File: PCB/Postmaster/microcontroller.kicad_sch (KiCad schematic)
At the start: 3 parts, among them U2 STM32F407VETx, Y1 TFOM50M4RWKCKT2T

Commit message: Update schematics
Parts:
- added U3: S25FL064LABMFI013, Package_SO:SOIC-8_5.23x5.23mm_P1.27mm, symbol Memory_Flash:W25Q16JVSS
- added Y2: CSTNE8M00G550000R0, Crystal:Resonator_SMD_Murata_CSTxExxV-3Pin_3.0x1.1mm, symbol Device:Resonator
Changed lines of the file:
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@@
 		(shape output)
 		(at 161.29 115.57 0)
+		(fields_autoplaced yes)
 		(effects
 			(font
@@
 		(shape output)
 		(at 184.15 41.91 0)
+		(fields_autoplaced yes)
 		(effects
 			(font
@@
 		(shape output)
 		(at 161.29 57.15 0)
+		(fields_autoplaced yes)
 		(effects
 			(font
@@
 		(shape output)
 		(at 161.29 110.49 0)
+		(fields_autoplaced yes)
 		(effects
 			(font
@@
 		(shape bidirectional)
 		(at 161.29 44.45 0)
+		(fields_autoplaced yes)
 		(effects
 			(font
@@
 		(shape output)
 		(at 161.29 113.03 0)
+		(fields_autoplaced yes)
 		(effects
 			(font
@@
 		(shape input)
 		(at 161.29 138.43 0)
+		(fields_autoplaced yes)
 		(effects
 			(font
@@
 		(shape input)
 		(at 161.29 135.89 0)
+		(fields_autoplaced yes)
 		(effects
 			(font
@@
 		(shape output)
 		(at 161.29 128.27 0)
-		(effects
-			(font
-				(size 1.27 1.27)
-			)
-			(justify left)
+		(fields_autoplaced yes)
+		(effects
+			(font
+				(size 1.27 1.27)
+			)
+			(justify left)
+		)
+	)
+	(symbol
+		(lib_id "Device:Resonator")
+		(at 205.74 92.71 0)
+		(unit 1)
+		(exclude_from_sim no)
+		(in_bom yes)
+		(on_board yes)
+		(dnp no)
+		(fields_autoplaced yes)
+		(property "Reference" "Y2"
+			(at 205.74 85.09 0)
+			(effects
+				(font
+					(size 1.27 1.27)
+				)
+			)
+		)
+		(property "Value" "CSTNE8M00G550000R0"
+			(at 205.74 87.63 0)
+			(effects
+				(font
+					(size 1.27 1.27)
+				)
+			)
+		)
+		(property "Footprint" "Crystal:Resonator_SMD_Murata_CSTxExxV-3Pin_3.0x1.1mm"
+			(at 205.105 92.71 0)
+			(effects
+				(font
+					(size 1.27 1.27)
+				)
+				(hide yes)
+			)
+		)
+		(property "Datasheet" "~"
+			(at 205.105 92.71 0)
+			(effects
+				(font
+					(size 1.27 1.27)
+				)
+				(hide yes)
+			)
+		)
+		(property "Description" "Three pin ceramic resonator"
+			(at 205.74 92.71 0)
+			(effects
+				(font
+					(size 1.27 1.27)
+				)
+				(hide yes)
+			)
+		)
+		(property "JLCPCBPart" "C341522"
+			(at 205.74 92.71 0)
+			(effects
+				(font
+					(size 1.27 1.27)
+				)
+				(hide yes)
+			)
+		)
+		(pin "2"
+		)
+		(pin "3"
+		)
+		(pin "1"
+		)
+		(instances
+			(project ""
+				(path "/b2fb7ca8-b44b-45c2-b25e-cd50f2bbc5c4/6b6c9333-359e-485e-9820-666d3b2f9ba5"
+					(reference "Y2")
+					(unit 1)
+				)
+			)
 		)
 	)
@@
 					(unit 1)
 				)
+			)
+		)
+	)
+	(symbol
+		(lib_id "Memory_Flash:W25Q16JVSS")
+		(at 208.28 127 0)
+		(unit 1)
+		(exclude_from_sim no)
+		(in_bom yes)
+		(on_board yes)
+		(dnp no)
+		(fields_autoplaced yes)
+		(property "Reference" "U3"
+			(at 217.17 125.7299 0)
+			(effects
+				(font
+					(size 1.27 1.27)
+				)
+				(justify left)
+			)
+		)
+		(property "Value" "S25FL064LABMFI013"
+			(at 217.17 128.2699 0)
+			(effects
+				(font
+					(size 1.27 1.27)
+				)
+				(justify left)
+			)
+		)
+		(property "Footprint" "Package_SO:SOIC-8_5.23x5.23mm_P1.27mm"
+			(at 208.28 127 0)
+			(effects
+				(font
+					(size 1.27 1.27)
+				)
+				(hide yes)
+			)
+		)
+		(property "Datasheet" "https://www.winbond.com/hq/support/documentation/levelOne.jsp?__locale=en&DocNo=DA00-W25Q16JV.1"
+			(at 208.28 127 0)
+			(effects
+				(font
+					(size 1.27 1.27)
+				)
+				(hide yes)
+			)
+		)
+		(property "Description" "16Mb Serial Flash Memory, Standard/Dual/Quad SPI, SOIC-8"
+			(at 208.28 127 0)
+			(effects
+				(font
+					(size 1.27 1.27)
+				)
+				(hide yes)
+			)
+		)
+		(property "JLCPCBPart" "C2951282"
+			(at 208.28 127 0)
+			(effects
+				(font
+					(size 1.27 1.27)
+				)
+				(hide yes)
+			)
+		)
+		(pin "6"
+		)
+		(pin "8"
+		)
+		(pin "1"
+		)
+		(pin "4"
+		)
+		(pin "3"
+		)
+		(pin "5"
+		)
+		(pin "7"
+		)
+		(pin "2"
+		)
+		(instances
+			(project ""
+				(path "/b2fb7ca8-b44b-45c2-b25e-cd50f2bbc5c4/6b6c9333-359e-485e-9820-666d3b2f9ba5"
+					(reference "U3")
+					(unit 1)
+				)

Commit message: Update schematics
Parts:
- added C16, C17: 2u2, Capacitor_SMD:C_0603_1608Metric, symbol Device:C
- added C18, C20, C21, C23, C24, C25, C26, C27: 100n, Capacitor_SMD:C_0603_1608Metric, symbol Device:C
- added C19, C22: 10u, Capacitor_SMD:C_0603_1608Metric, symbol Device:C
- added J1: Conn_01x02, Connector_PinSocket_2.54mm:PinSocket_1x02_P2.54mm_Vertical, symbol Connector_Generic:Conn_01x02
- added J2: Conn_02x08_Odd_Even, Connector_PinHeader_2.54mm:PinHeader_2x08_P2.54mm_Vertical, symbol Connector_Generic:Conn_02x08_Odd_Even
- added J3, J4: Conn_01x04, Connector_PinHeader_2.54mm:PinHeader_1x04_P2.54mm_Vertical, symbol Connector_Generic:Conn_01x04
- added J5: Conn_01x03, Connector_PinHeader_2.54mm:PinHeader_1x03_P2.54mm_Vertical, symbol Connector_Generic:Conn_01x03
- added J6: Conn_02x10_Odd_Even, Connector_IDC:IDC-Header_2x10_P2.54mm_Vertical, symbol Connector_Generic:Conn_02x10_Odd_Even
- added R17, R18: 2k2, Resistor_SMD:R_0603_1608Metric, symbol Device:R
- U2: JLCPCBPart C28730 -> (none)
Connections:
- net +3.3V: now also U2.100 (VDD), U2.11 (VDD), U2.19 (VDD), U2.21 (VREF+), U2.22 (VDDA), U2.28 (VDD), U2.50 (VDD), U2.6 (VBAT), U2.75 (VDD), U3.3 (IO2), U3.7 (IO3), U3.8 (VCC), C18.1, C19.1, C20.1, C21.1, C22.1, C23.1, C24.1, C25.1, C26.1, J2.7 (Pin_7), J4.2 (Pin_2), J6.1 (Pin_1), J6.2 (Pin_2), R17.1, R18.1
- net GND: now also U2.10 (VSS), U2.20 (VSSA), U2.27 (VSS), U2.74 (VSS), U2.94 (BOOT0), U2.99 (VSS), U3.4 (GND), Y2.2, C16.2, C17.2, C18.2, C19.2, C20.2, C21.2, C22.2, C23.2, C24.2, C25.2, C26.2, C27.2, J2.13 (Pin_13), J4.1 (Pin_1), J5.1 (Pin_1), J6.10 (Pin_10), J6.12 (Pin_12), J6.14 (Pin_14), J6.16 (Pin_16), J6.18 (Pin_18), J6.20 (Pin_20), J6.4 (Pin_4), J6.6 (Pin_6), J6.8 (Pin_8)
- net at Y2.1: now also U2.12 (PH0)
- net at Y2.3: now also U2.13 (PH1)
- net FLASH_CS: now reaches U3.1 (~{CS})
- net FLASH_CS: now also U2.77 (PA15)
- net SPI3_MISO: now reaches U3.2 (DO(IO1))
- net SPI3_MISO: now also U2.79 (PC11)
- net SPI3_MOSI: now reaches U3.5 (DI(IO0))
- net SPI3_MOSI: now also U2.80 (PC12)
- net SPI3_CLK: now reaches U3.6 (CLK)
- net SPI3_CLK: now also U2.78 (PC10)
- net RESET: now reaches U2.14 (NRST)
- net RESET: now also C27.1, J6.15 (Pin_15)
- net at U2.49 (VCAP_1): now also C17.1
- net UART3_TX: now reaches U2.55 (PD8)
- net UART3_TX: now also J6.17 (Pin_17)
- net UART3_RX: now reaches U2.56 (PD9)
- net UART3_RX: now also J6.5 (Pin_5)
- net STLINK_RX: now reaches U2.64 (PC7)
- net STLINK_RX: now also J1.1 (Pin_1)
- net ALT_UART1_TX: now reaches U2.68 (PA9)
- net ALT_UART1_TX: now also J5.2 (Pin_2)
- net at U2.69 (PA10): now also J2.6 (Pin_6)
- net SWDIO: now reaches U2.72 (PA13)
- net SWDIO: now also J6.7 (Pin_7)
- net at U2.73 (VCAP_2): now also C16.1
- net SWCLK: now reaches U2.76 (PA14)
- net SWCLK: now also J6.9 (Pin_9)
- net SWO: now reaches U2.89 (PB3)
- net SWO: now also J6.13 (Pin_13)
- net at U2.90 (PB4): now also J2.5 (Pin_5)
- net BOOT0: now reaches U2.91 (PB5)
- net BOOT0: now also J3.2 (Pin_2)
- net at U2.92 (PB6): now also J2.8 (Pin_8)
- net ALT_UART1_RX: now reaches U2.93 (PB7)
- net ALT_UART1_RX: now also J5.3 (Pin_3)
- net SCK: now reaches U2.95 (PB8)
- net SCK: now also J4.3 (Pin_3), R17.2
- net SDA: now reaches U2.96 (PB9)
- net SDA: now also J4.4 (Pin_4), R18.2
- no-connect marks 0 -> 71
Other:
- moved on the sheet: U3, Y2

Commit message: Update schematics
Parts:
- added SW1: SW_MEC_5E, Button_Switch_SMD:SW_SPST_TL3305B, symbol Switch:SW_MEC_5E
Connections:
- net GND: now also SW1.1, SW1.2
- net RESET: now also SW1.3 (K), SW1.4 (A)
- net TRESET: now reaches J2.5 (Pin_5), U2.90 (PB4)
- net UART1_RX: now reaches J2.6 (Pin_6), U2.69 (PA10)
- net UART1_TX: now reaches J2.8 (Pin_8), U2.92 (PB6)
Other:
- moved on the sheet: C20, C27, J1, J2, J3, J5, J6, U3, Y2

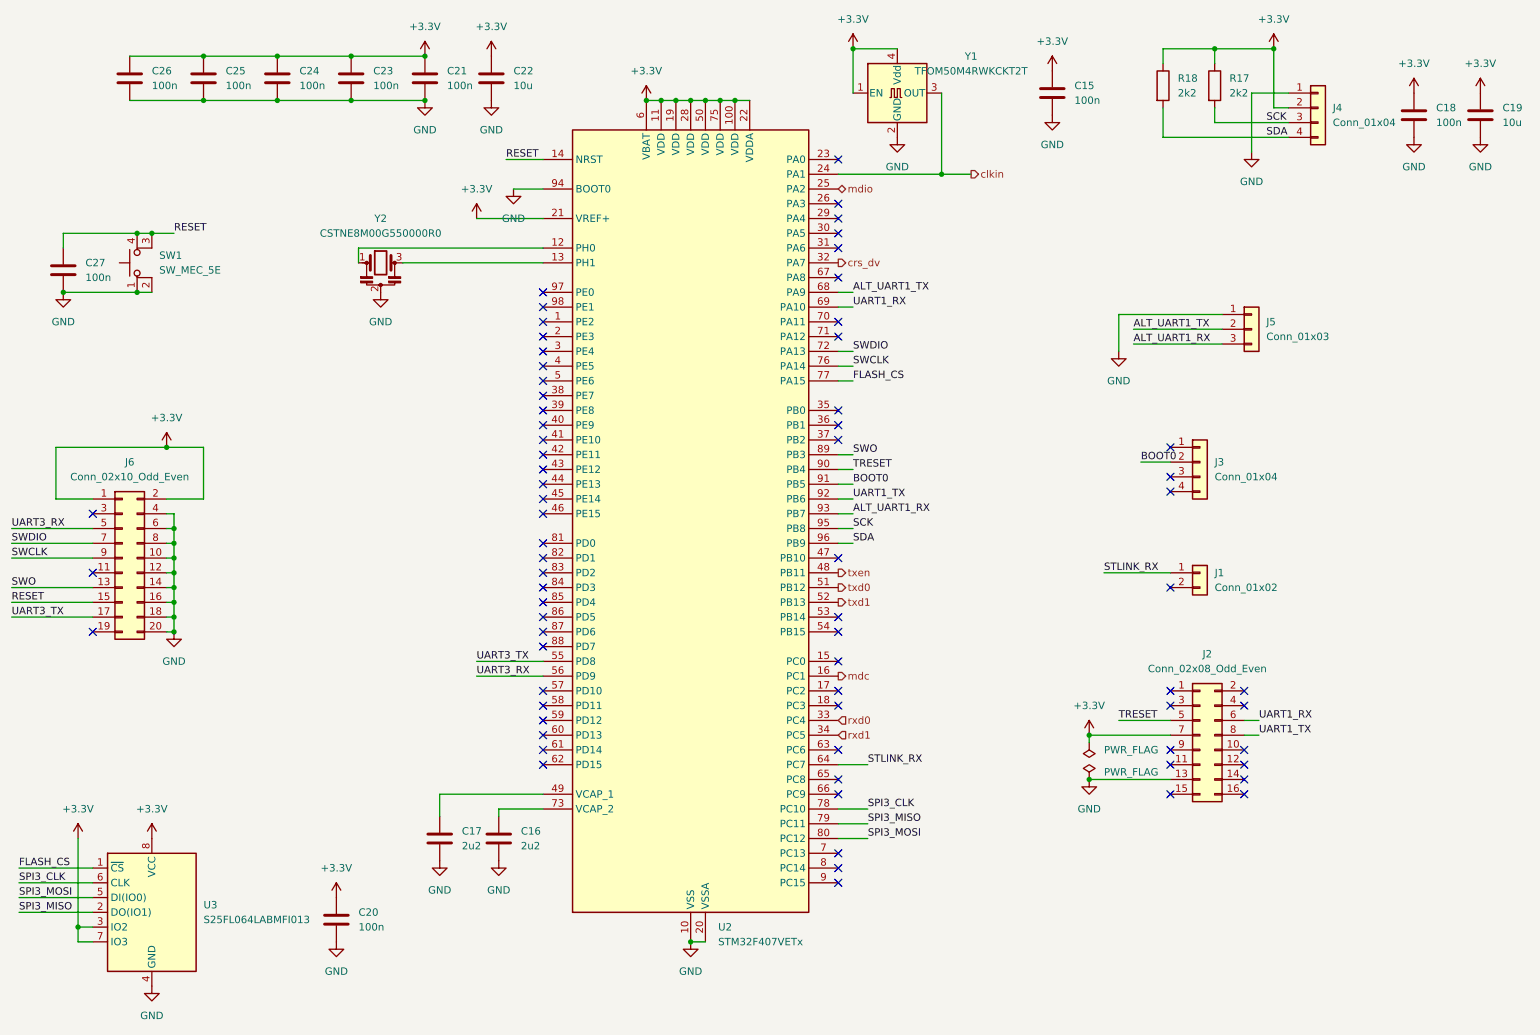
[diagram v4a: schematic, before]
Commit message: Update schematics, add production files
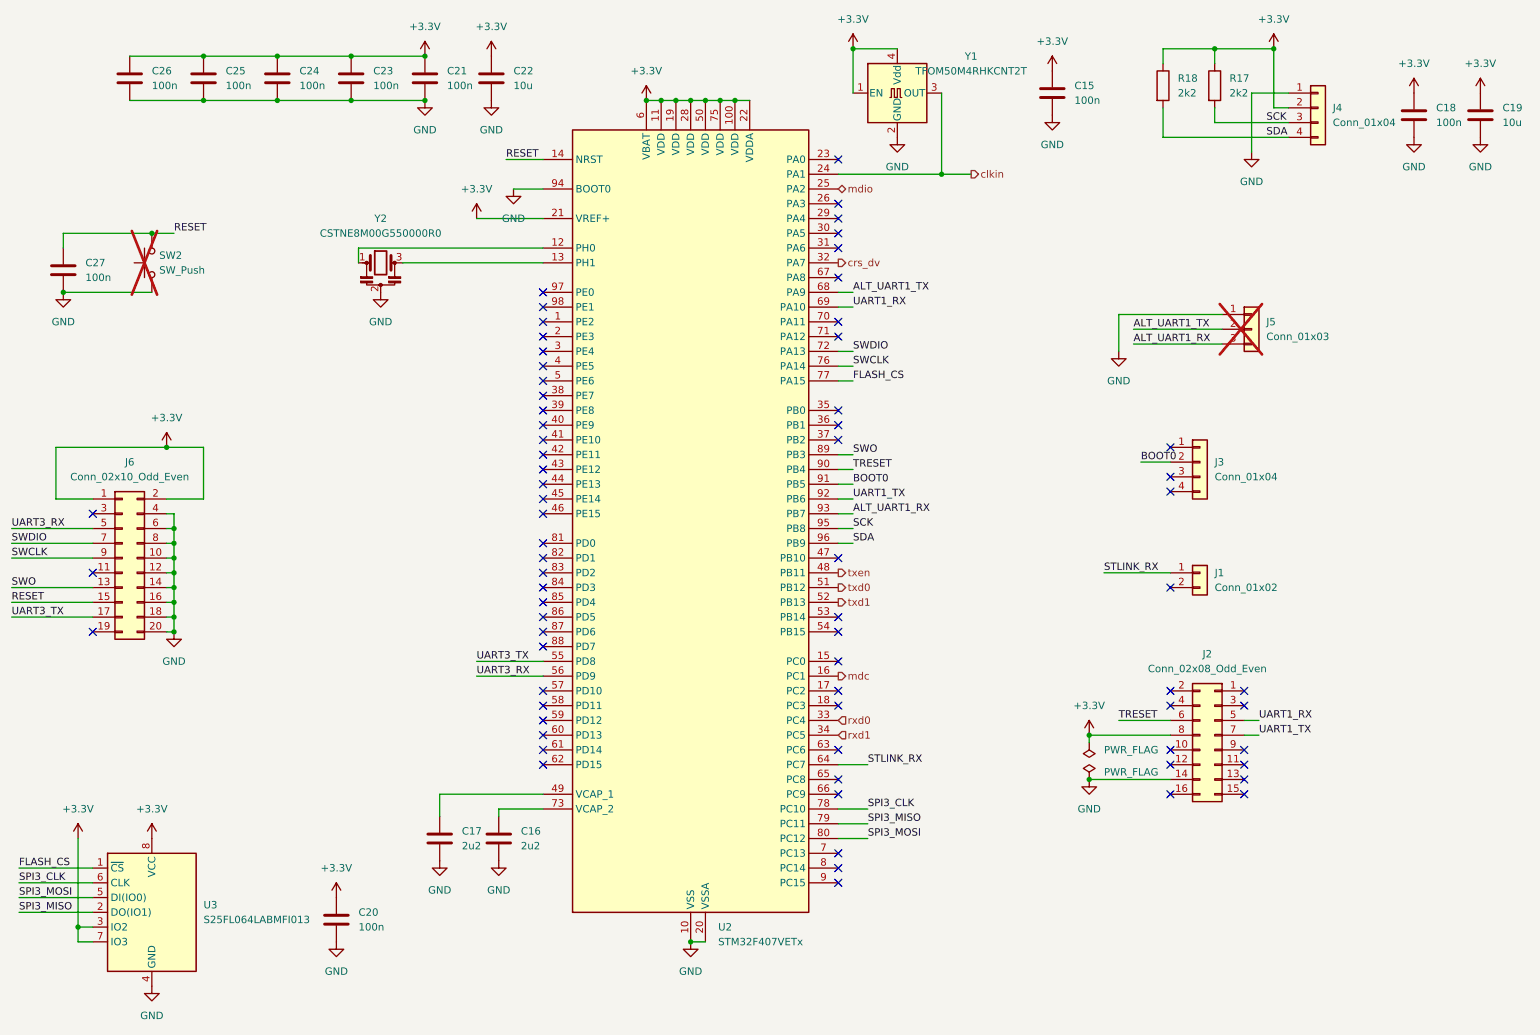
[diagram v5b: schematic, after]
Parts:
- removed SW1: SW_MEC_5E, Button_Switch_SMD:SW_SPST_TL3305B, symbol Switch:SW_MEC_5E
- added SW2: SW_Push, Button_Switch_SMD:SW_SPST_TL3305B, symbol Switch:SW_Push
- J3, J4: JLCPCBPart C6332197 -> C7430360
- J5: now not fitted
- U2: JLCPCBPart (none) -> C28730
- Y1: value TFOM50M4RWKCKT2T -> TFOM50M4RHKCNT2T; footprint Oscillator:Oscillator_SMD_ECS_2520MV-xxx-xx-4Pin_2.5x2.0mm -> Oscillator:Oscillator_SMD_Abracon_ASE-4Pin_3.2x2.5mm; JLCPCBPart C2992633 -> C454615
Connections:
- net +3.3V: now also J2.8 (Pin_8); no longer J2.7 (Pin_7)
- net GND: now also J2.14 (Pin_14), SW2.1; no longer J2.13 (Pin_13)
- net RESET: now also SW2.2
- net TRESET: now also J2.6 (Pin_6); no longer J2.5 (Pin_5)
- net UART1_RX: now also J2.5 (Pin_5); no longer J2.6 (Pin_6)
- net UART1_TX: now also J2.7 (Pin_7); no longer J2.8 (Pin_8)
